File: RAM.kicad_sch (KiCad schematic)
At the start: 7 parts

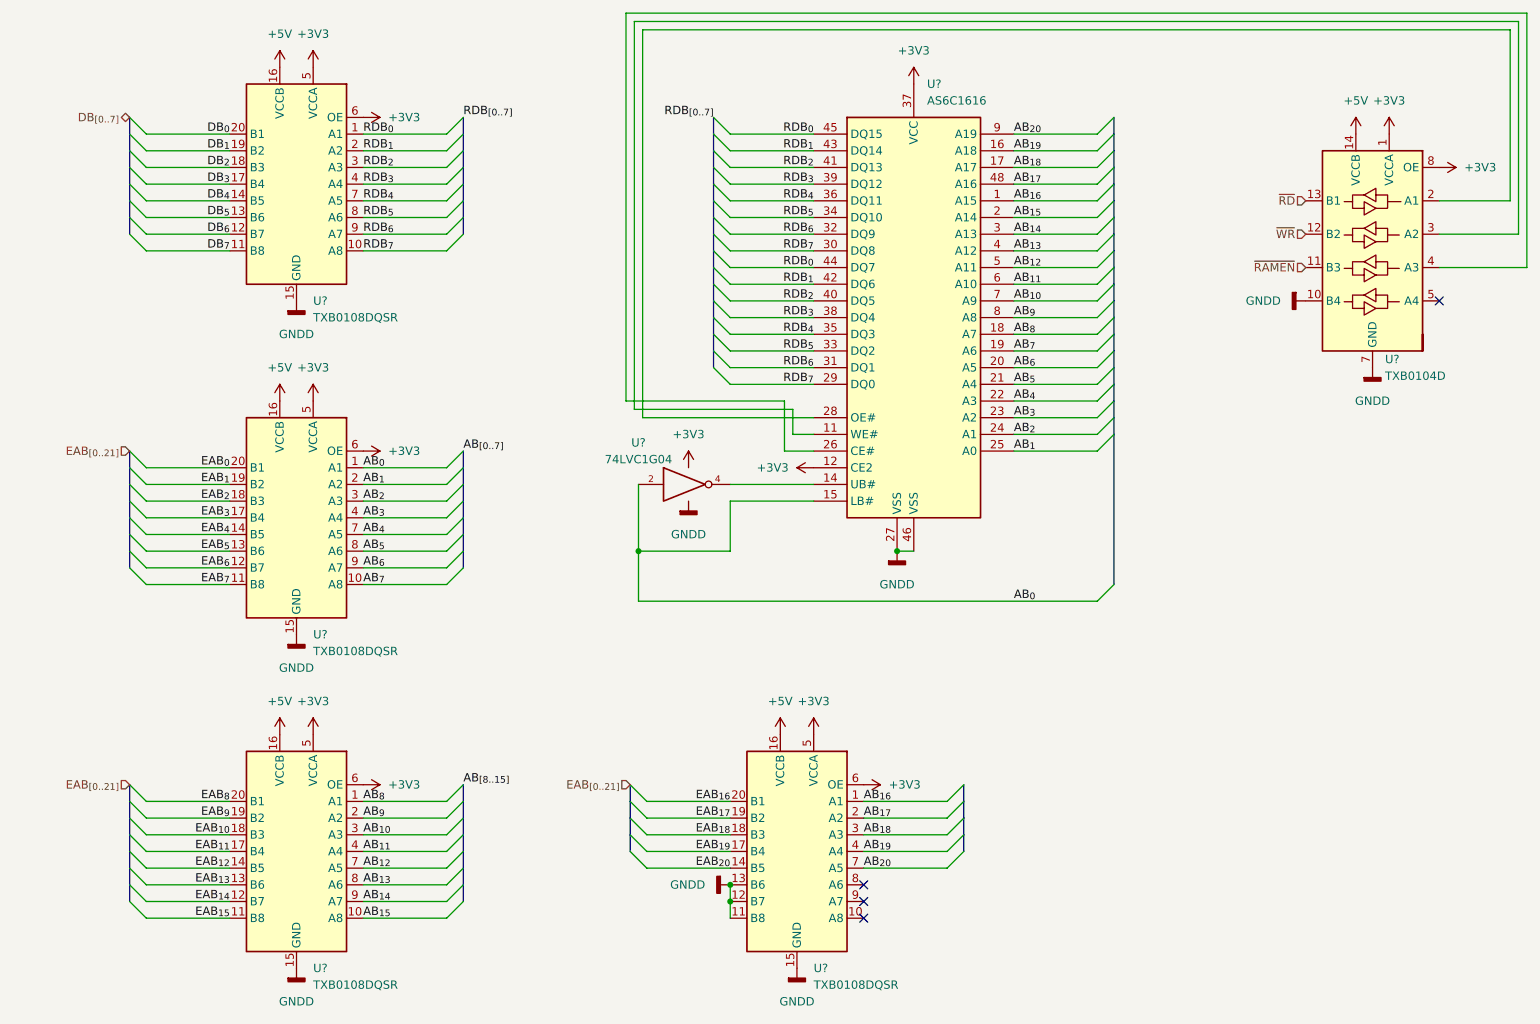
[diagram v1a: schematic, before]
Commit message: changed bus names to avoid possible conflicts, fixed unnamed busses.
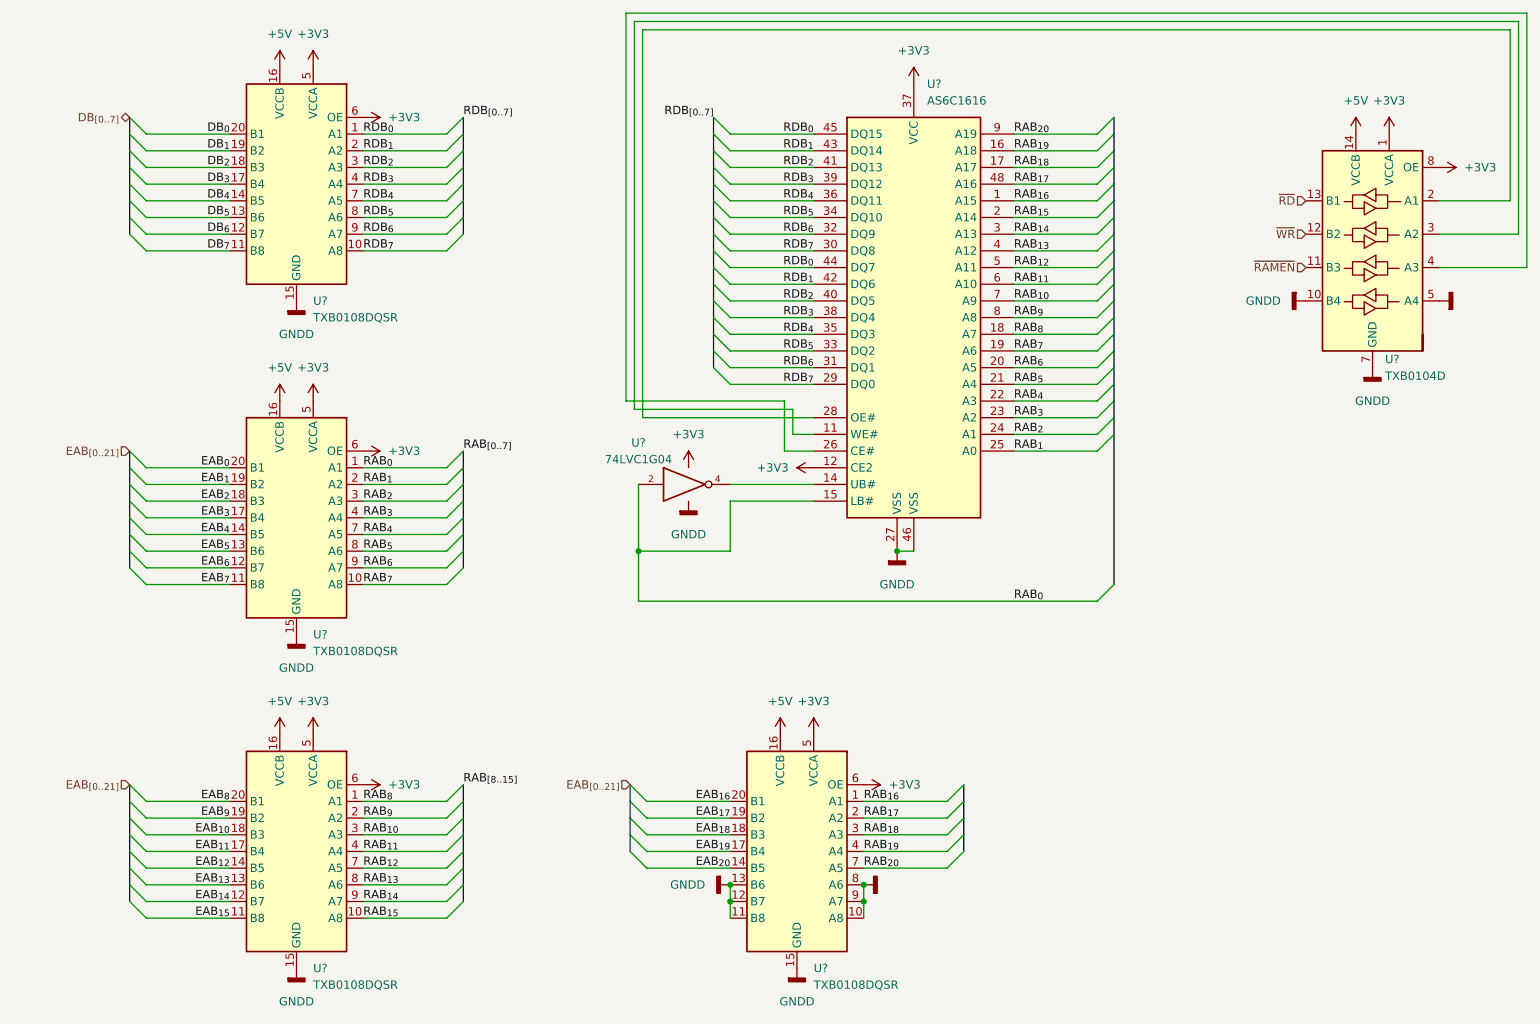
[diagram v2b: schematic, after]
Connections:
- net GND: now also U?.10 (A8), U?.5 (A4), U?.8 (A6), U?.9 (A7)
- net AB_{0} renamed RAB_{0}
- net AB_{10} renamed RAB_{10}
- net AB_{11} renamed RAB_{11}
- net AB_{12} renamed RAB_{12}
- net AB_{13} renamed RAB_{13}
- net AB_{14} renamed RAB_{14}
- net AB_{15} renamed RAB_{15}
- net AB_{16} renamed RAB_{16}
- net AB_{17} renamed RAB_{17}
- net AB_{18} renamed RAB_{18}
- net AB_{19} renamed RAB_{19}
- net AB_{1} renamed RAB_{1}
- net AB_{20} renamed RAB_{20}
- net AB_{2} renamed RAB_{2}
- net AB_{3} renamed RAB_{3}
- net AB_{4} renamed RAB_{4}
- net AB_{5} renamed RAB_{5}
- net AB_{6} renamed RAB_{6}
- net AB_{7} renamed RAB_{7}
- net AB_{8} renamed RAB_{8}
- net AB_{9} renamed RAB_{9}
- no-connect marks 4 -> 0

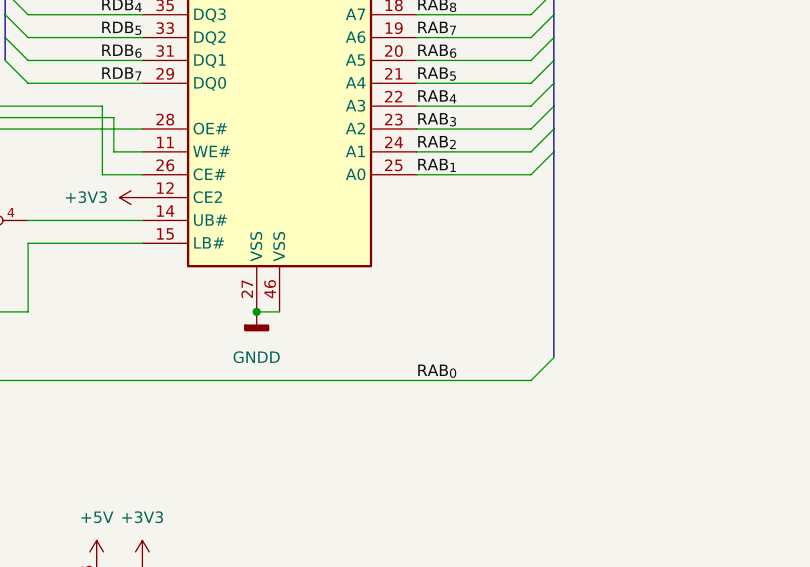
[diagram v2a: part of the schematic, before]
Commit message: added decoupling capacitors, perhaps too many? idk better more than less!
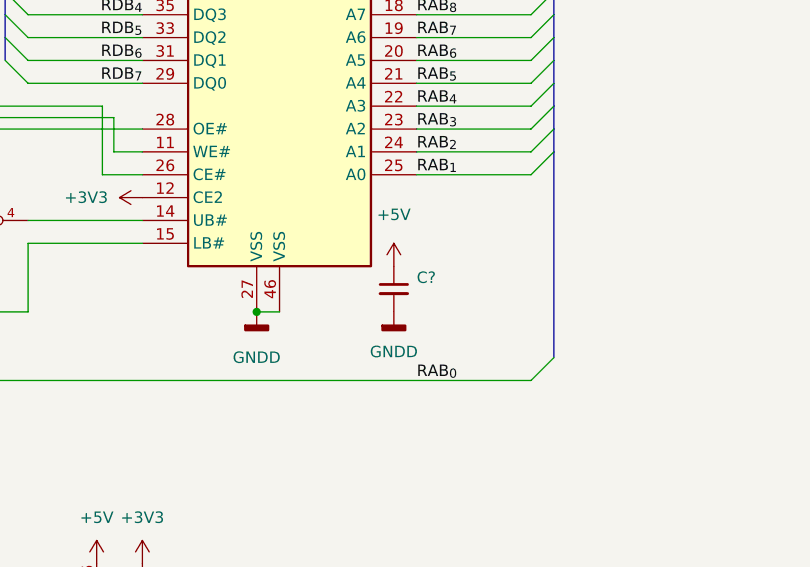
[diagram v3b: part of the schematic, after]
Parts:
- added C?: (no value), symbol Device:C_Small
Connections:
- net +5V: now also C?.1
- net GND: now also C?.2
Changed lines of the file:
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@@
+    (pin "1")
+  )
+  (symbol (lib_id "power:+5V") (at 154.94 96.52 0) (unit 1)
+    (in_bom yes) (on_board yes) (fields_autoplaced)
+    (property "Reference" "#PWR?" (id 0) (at 154.94 100.33 0)
+      (effects (font (size 1.27 1.27)) hide)
+    )
+    (property "Value" "+5V" (id 1) (at 154.94 90.805 0))
+    (property "Footprint" "" (id 2) (at 154.94 96.52 0)
+      (effects (font (size 1.27 1.27)) hide)
+    )
+    (property "Datasheet" "" (id 3) (at 154.94 96.52 0)
+      (effects (font (size 1.27 1.27)) hide)
+    )
     (pin "1")
   )
@@
     (pin "1")
   )
+  (symbol (lib_id "Device:C_Small") (at 154.94 99.06 0) (unit 1)
+    (in_bom yes) (on_board yes) (fields_autoplaced)
+    (property "Reference" "C?" (id 0) (at 157.48 97.7962 0)
+      (effects (font (size 1.27 1.27)) (justify left))
+    )
+    (property "Value" "" (id 1) (at 157.48 100.3362 0)
+      (effects (font (size 1.27 1.27)) (justify left))
+    )
+    (property "Footprint" "" (id 2) (at 154.94 99.06 0)
+      (effects (font (size 1.27 1.27)) hide)
+    )
+    (property "Datasheet" "~" (id 3) (at 154.94 99.06 0)
+      (effects (font (size 1.27 1.27)) hide)
+    )
+    (pin "1")
+    (pin "2")
+  )
   (symbol (lib_id "power:GNDD") (at 212.09 73.66 0) (unit 1)
     (in_bom yes) (on_board yes) (fields_autoplaced)
@@
       (effects (font (size 1.27 1.27)) hide)
     )
+    (pin "1")
+  )
+  (symbol (lib_id "power:GNDD") (at 154.94 101.6 0) (unit 1)
+    (in_bom yes) (on_board yes) (fields_autoplaced)
+    (property "Reference" "#PWR?" (id 0) (at 154.94 107.95 0)
+      (effects (font (size 1.27 1.27)) hide)
+    )
+    (property "Value" "GNDD" (id 1) (at 154.94 106.045 0))
+    (property "Footprint" "" (id 2) (at 154.94 101.6 0)
+      (effects (font (size 1.27 1.27)) hide)
+    )
+    (property "Datasheet" "" (id 3) (at 154.94 101.6 0)
+      (effects (font (size 1.27 1.27)) hide)
+    )

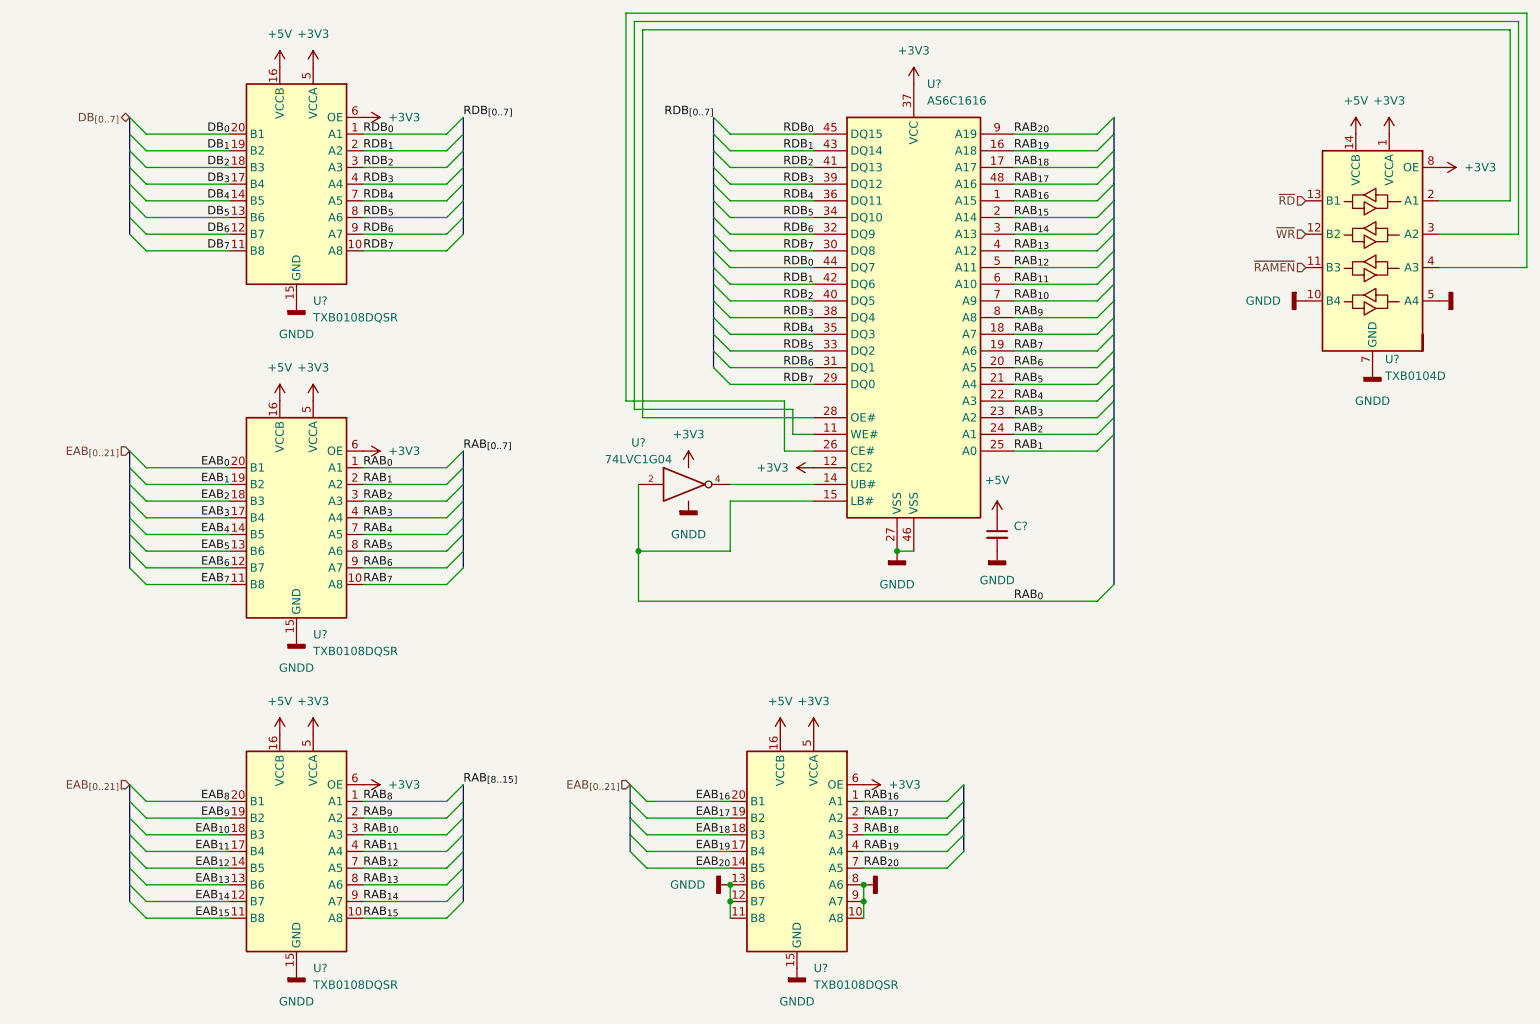
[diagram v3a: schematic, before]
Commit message: some clean up and simplification, as well as some renaming
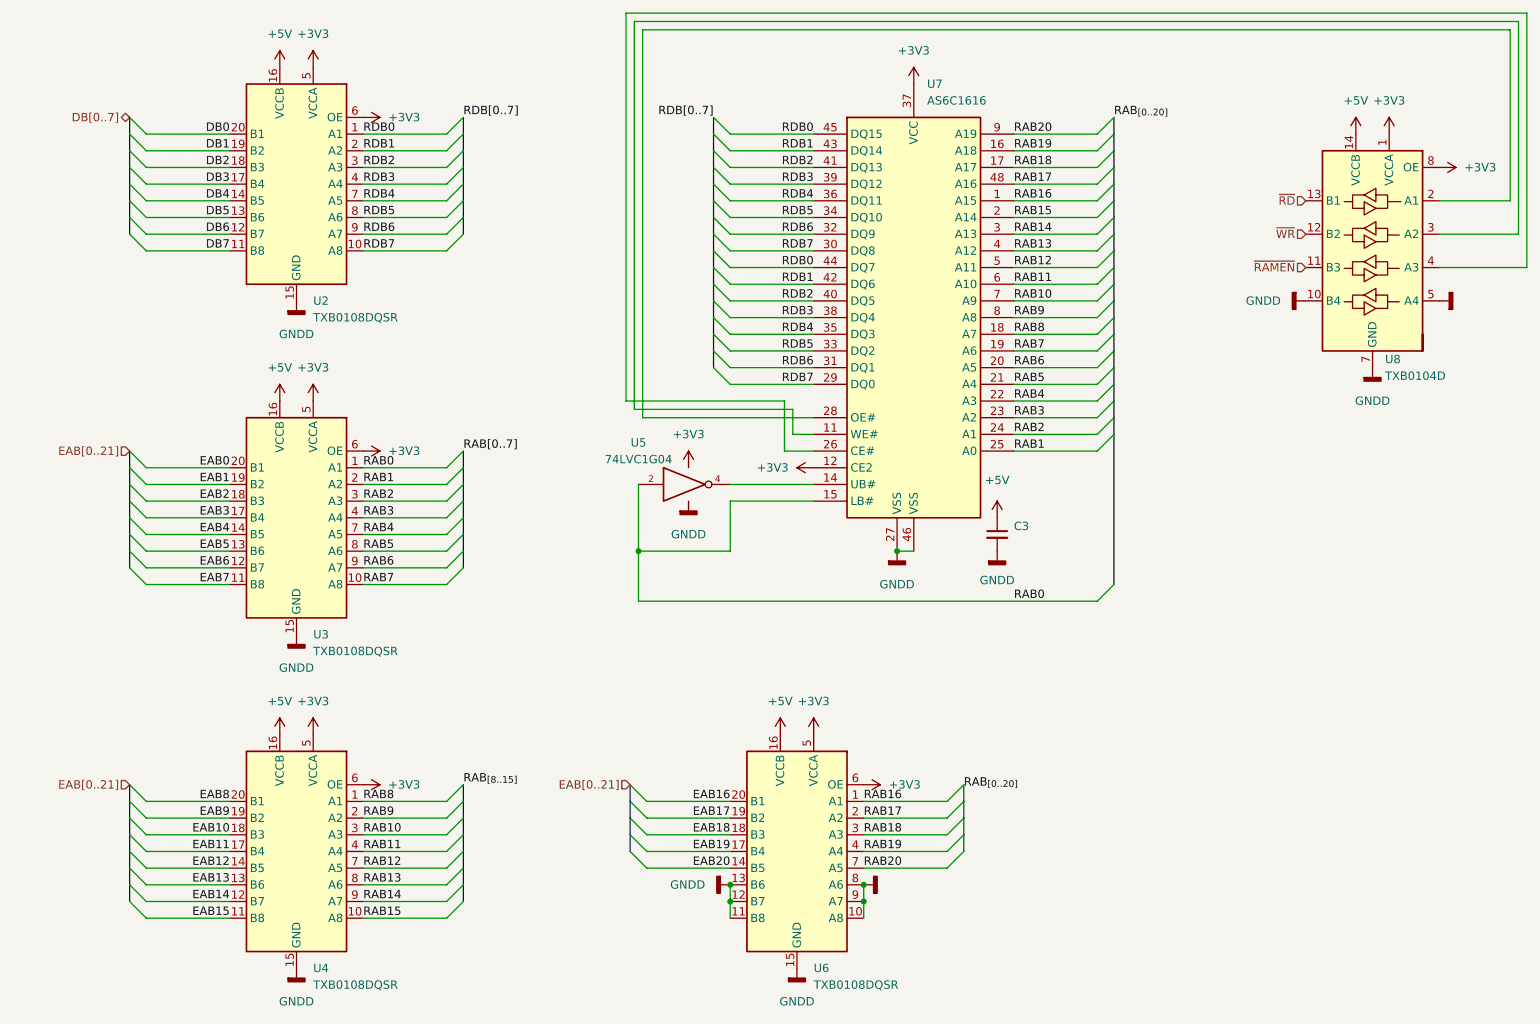
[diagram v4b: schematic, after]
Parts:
- gave numbers to parts that had none: 8
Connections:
- net DB_{0} renamed DB0
- net DB_{1} renamed DB1
- net DB_{2} renamed DB2
- net DB_{3} renamed DB3
- net DB_{4} renamed DB4
- net DB_{5} renamed DB5
- net DB_{6} renamed DB6
- net DB_{7} renamed DB7
- net EAB_{0} renamed EAB0
- net EAB_{10} renamed EAB10
- net EAB_{11} renamed EAB11
- net EAB_{12} renamed EAB12
- net EAB_{13} renamed EAB13
- net EAB_{14} renamed EAB14
- net EAB_{15} renamed EAB15
- net EAB_{16} renamed EAB16
- net EAB_{17} renamed EAB17
- net EAB_{18} renamed EAB18
- net EAB_{19} renamed EAB19
- net EAB_{1} renamed EAB1
- net EAB_{20} renamed EAB20
- net EAB_{2} renamed EAB2
- net EAB_{3} renamed EAB3
- net EAB_{4} renamed EAB4
- net EAB_{5} renamed EAB5
- net EAB_{6} renamed EAB6
- net EAB_{7} renamed EAB7
- net EAB_{8} renamed EAB8
- net EAB_{9} renamed EAB9
- net RAB_{0} renamed RAB0
- net RAB_{10} renamed RAB10
- net RAB_{11} renamed RAB11
- net RAB_{12} renamed RAB12
- net RAB_{13} renamed RAB13
- net RAB_{14} renamed RAB14
- net RAB_{15} renamed RAB15
- net RAB_{16} renamed RAB16
- net RAB_{17} renamed RAB17
- net RAB_{18} renamed RAB18
- net RAB_{19} renamed RAB19
- net RAB_{1} renamed RAB1
- net RAB_{20} renamed RAB20
- net RAB_{2} renamed RAB2
- net RAB_{3} renamed RAB3
- net RAB_{4} renamed RAB4
- net RAB_{5} renamed RAB5
- net RAB_{6} renamed RAB6
- net RAB_{7} renamed RAB7
- net RAB_{8} renamed RAB8
- net RAB_{9} renamed RAB9
- net RDB_{0} renamed RDB0
- net RDB_{1} renamed RDB1
- net RDB_{2} renamed RDB2
- net RDB_{3} renamed RDB3
- net RDB_{4} renamed RDB4
- net RDB_{5} renamed RDB5
- net RDB_{6} renamed RDB6
- net RDB_{7} renamed RDB7
